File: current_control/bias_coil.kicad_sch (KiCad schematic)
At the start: 45 parts, among them J1 Conn_01x10_Pin, J10 Conn_Coaxial, J11 Conn_Coaxial, J13 Screw_Terminal_01x02, J2 Conn_01x10_Pin, J4 Conn_01x05, J6 Conn_Coaxial, J7 Conn_Coaxial, J8 Conn_Coaxial, J9 Conn_Coaxial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

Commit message: add production files for current control pcb
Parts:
- C1, C2, C3: LCSC (none) -> C5632429
- C10, C11, C5, C7: LCSC (none) -> C5632437
- C4, C6, C8, C9: LCSC (none) -> C2761733
- D1, D2, D3: LCSC (none) -> C895238
- J13: LCSC (none) -> C8465
- R1, R2, R6: LCSC (none) -> C119304
- R10, R11, R12: LCSC (none) -> C713997
- R3, R4, R5: LCSC (none) -> C410695
- U3, U4, U5: LCSC (none) -> C727603
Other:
- title: ??? -> 3 Channel current driver

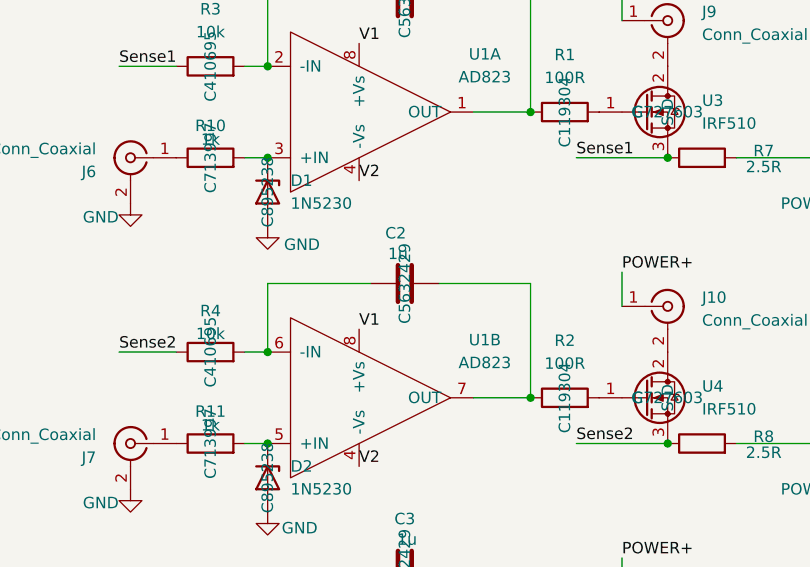
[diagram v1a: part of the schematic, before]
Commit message: updated 3-channel H-bridge
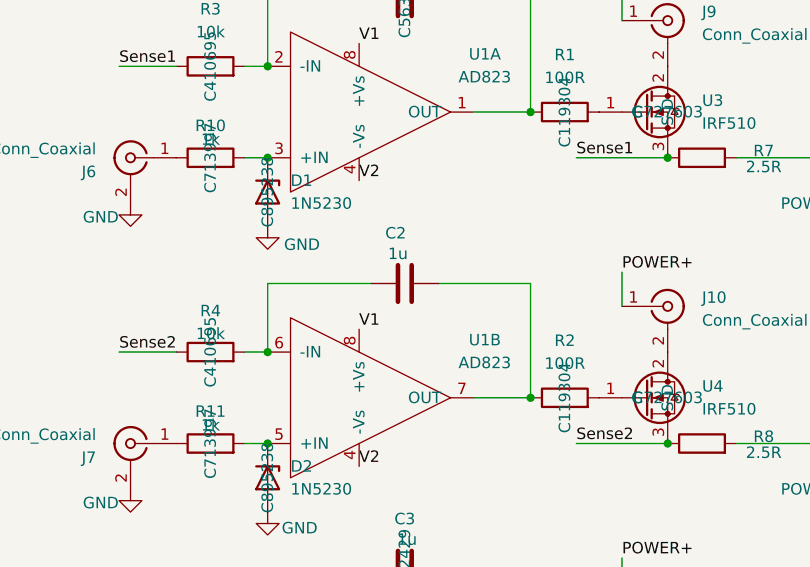
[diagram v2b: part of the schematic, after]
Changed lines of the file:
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@@
 					(size 1.27 1.27)
 				)
+				(hide yes)
 			)
 		)
